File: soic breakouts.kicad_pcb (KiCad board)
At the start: 2 copper layers, 128.4 x 76 mm, 106 parts, among them J1 Conn_01x07, J2 Conn_01x07, J3 Conn_01x01, J4 Conn_01x08, J5 Conn_01x08, J6 Conn_01x01, U1 TL074, U2 LM13700

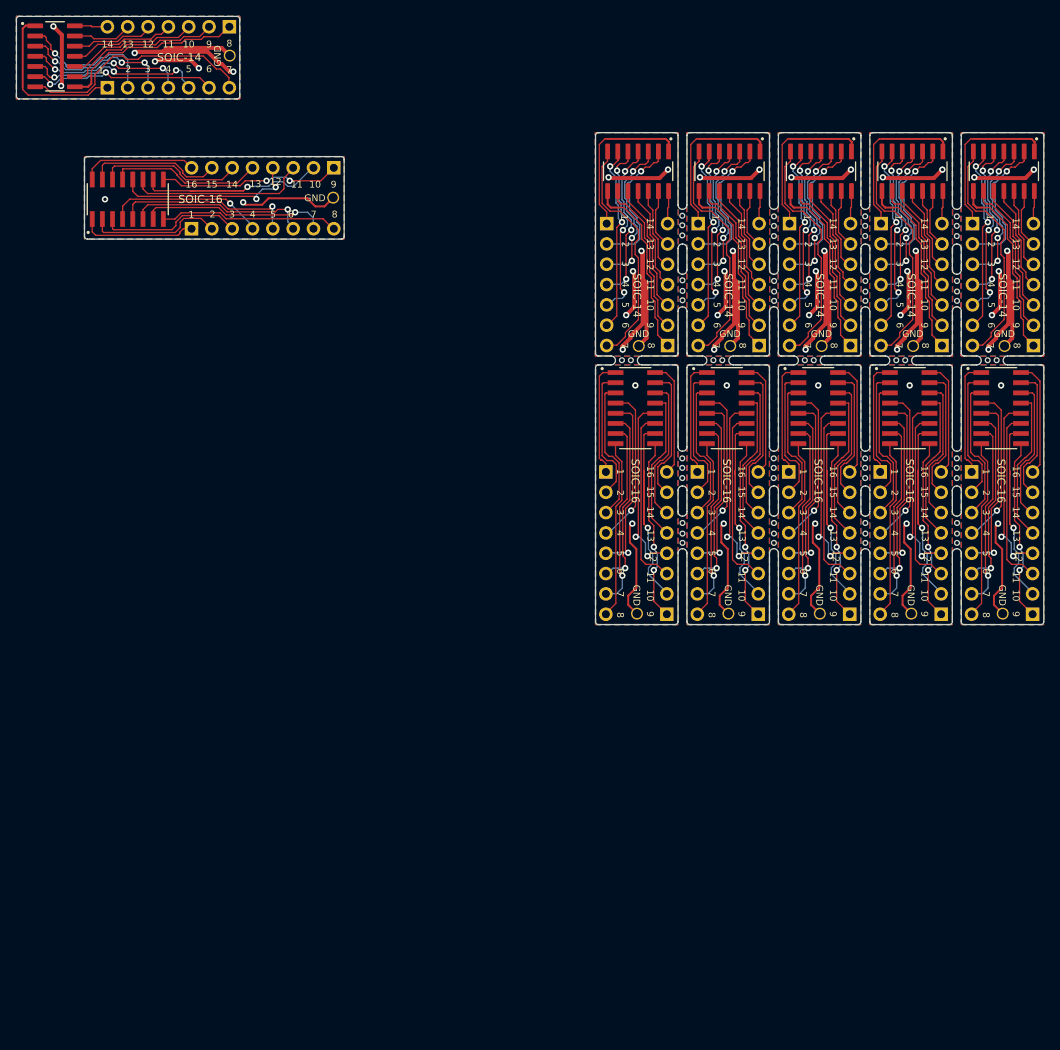
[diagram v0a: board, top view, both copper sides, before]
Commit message: Add SOIC-8.
* Update to KiCAD 8 format.
* Add SOIC-8 footprint breakout.
* Update to new IPC pin 1 (triangle/arrow) indicator throughout.
* Make pin 1 on header more obvious with IPC indicator throughout.
* Increase silkscreen font size for main label per breakout board.
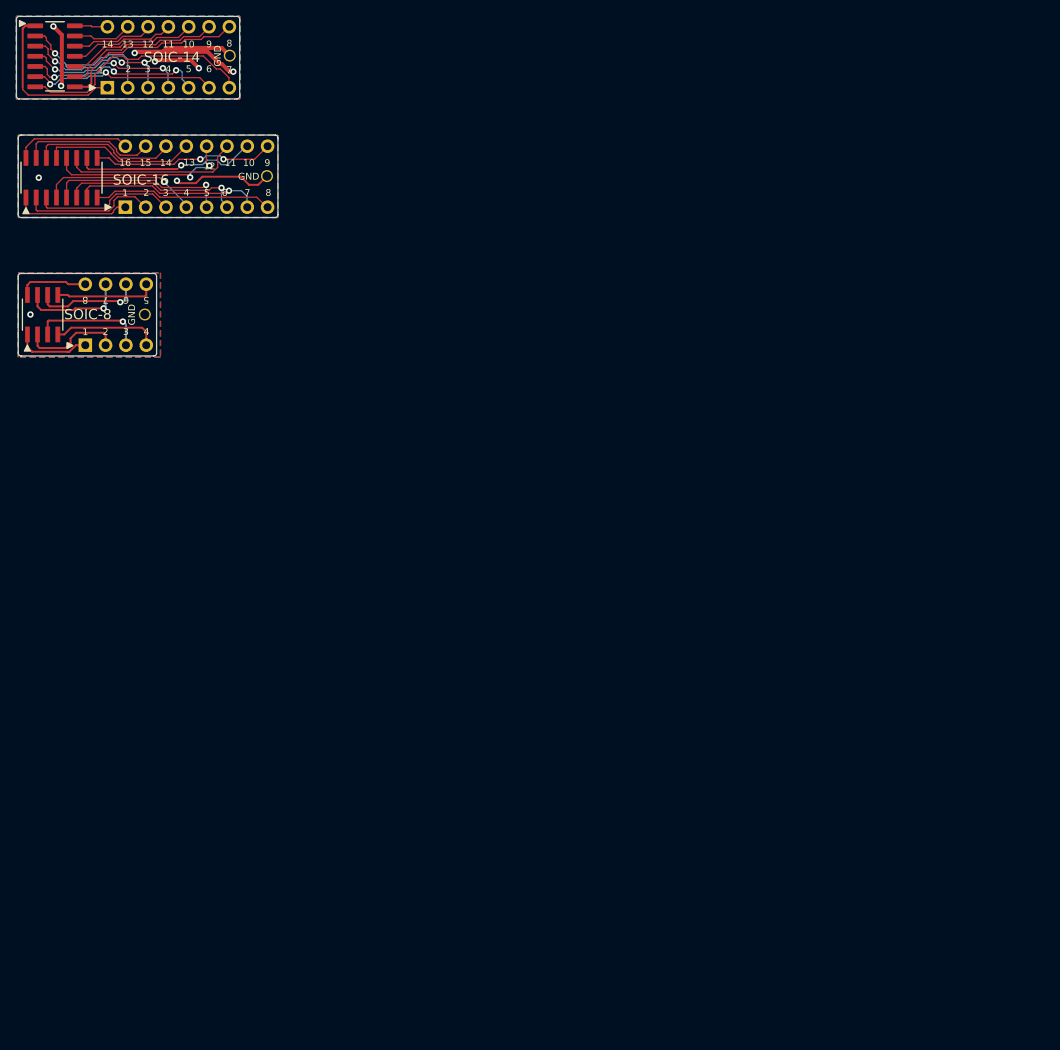
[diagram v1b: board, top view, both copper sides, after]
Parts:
- removed the J1 at (103.0, 41.9)
- removed the J1 at (137.3, 41.9)
- removed the J1 at (91.6, 41.9)
- removed the J1 at (125.9, 41.9)
- removed the J1 at (114.5, 41.9)
- removed the J2 at (133.5, 57.1)
- removed the J2 at (122.1, 57.1)
- removed the J2 at (144.9, 57.1)
- removed the J2 at (99.2, 57.1)
- removed the J2 at (110.6, 57.1)
- removed the J3 at (141.3, 57.1)
- removed the J3 at (129.9, 57.1)
- removed the J3 at (95.6, 57.1)
- removed the J3 at (118.5, 57.1)
- removed the J3 at (107.0, 57.1)
- removed the J4 at (102.9, 72.9)
- removed the J4 at (137.2, 72.9)
- removed the J4 at (114.4, 72.9)
- removed the J4 at (91.5, 72.9)
- removed the J4 at (125.8, 72.9)
- removed the J5 at (110.5, 90.7)
- removed the J5 at (133.4, 90.7)
- removed the J5 at (122.0, 90.7)
- removed the J5 at (99.1, 90.7)
- removed the J5 at (144.8, 90.7)
- removed the J6 at (95.4, 90.6)
- removed the J6 at (129.7, 90.6)
- removed the J6 at (118.2, 90.6)
- removed the J6 at (106.8, 90.6)
- removed the J6 at (141.1, 90.6)
- removed REF** (x58): MountingHole_80mil, Aaron_Pads:MountingHole_80mil
- removed the U1 at (129.8, 35.3)
- removed the U1 at (95.5, 35.3)
- removed the U1 at (106.9, 35.3)
- removed the U1 at (141.2, 35.3)
- removed the U1 at (118.4, 35.3)
- removed the U2 at (106.6, 64.9)
- removed the U2 at (140.9, 64.9)
- removed the U2 at (118.0, 64.9)
- removed the U2 at (95.2, 64.9)
- removed the U2 at (129.5, 64.9)
- added J7: Conn_01x01, Aaron_Pads:TP_HeaderPin_P2.54mm_round, F.Cu at (33.9, 53.2)
- added J8: Conn_01x04, Connector_PinHeader_2.54mm:PinHeader_1x04_P2.54mm_Vertical, F.Cu at (26.4, 49.4)
- added J9: Conn_01x04, Connector_PinHeader_2.54mm:PinHeader_1x04_P2.54mm_Vertical, F.Cu at (26.4, 57.0)
- added U3: TL072, Aaron_TI_Parts:TI_SOIC_D_R-PDSO-8, F.Cu at (21.1, 53.2)
- moved J4 8.71 mm to (31.4, 39.8)
- moved J5 8.71 mm to (49.2, 32.2)
- moved J6 8.71 mm to (49.1, 35.9)
- moved U2 8.71 mm to (23.4, 36.1)
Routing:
- net /GND1: track 235.1 -> 39.2 mm, vias 36 -> 6
- net Net-(J1-Pin_7): track 178.9 -> 29.8 mm
- net Net-(J5-Pin_2): track 176.3 -> 29.4 mm, vias 6 -> 1
- net Net-(J1-Pin_6): track 144.9 -> 24.2 mm, vias 12 -> 2
- net Net-(J4-Pin_7): track 137.1 -> 22.8 mm, vias 6 -> 1
- net Net-(J5-Pin_4): track 136.6 -> 22.8 mm, vias 12 -> 2
- net Net-(J2-Pin_1): track 135.8 -> 22.6 mm
- net Net-(J4-Pin_5): track 133.3 -> 22.2 mm, vias 6 -> 1
- net Net-(J1-Pin_5): track 133.1 -> 22.2 mm, vias 18 -> 3
- net Net-(J5-Pin_1): track 133.1 -> 22.2 mm, vias 12 -> 2
- net Net-(J4-Pin_6): track 132.3 -> 22.0 mm, vias 6 -> 1
- net Net-(J5-Pin_3): track 131.8 -> 22.0 mm
- net Net-(J4-Pin_8): track 130.7 -> 21.8 mm
- net Net-(J1-Pin_1): track 123.3 -> 20.6 mm
- net Net-(J1-Pin_4): track 121.9 -> 20.3 mm, vias 18 -> 3
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- added copper zone on B.Cu, net /GND3
- added copper zone on F.Cu, net /GND3
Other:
- board size 128.4 x 76 mm -> 32.7 x 42.4 mm
- board text added: "SOIC-8"

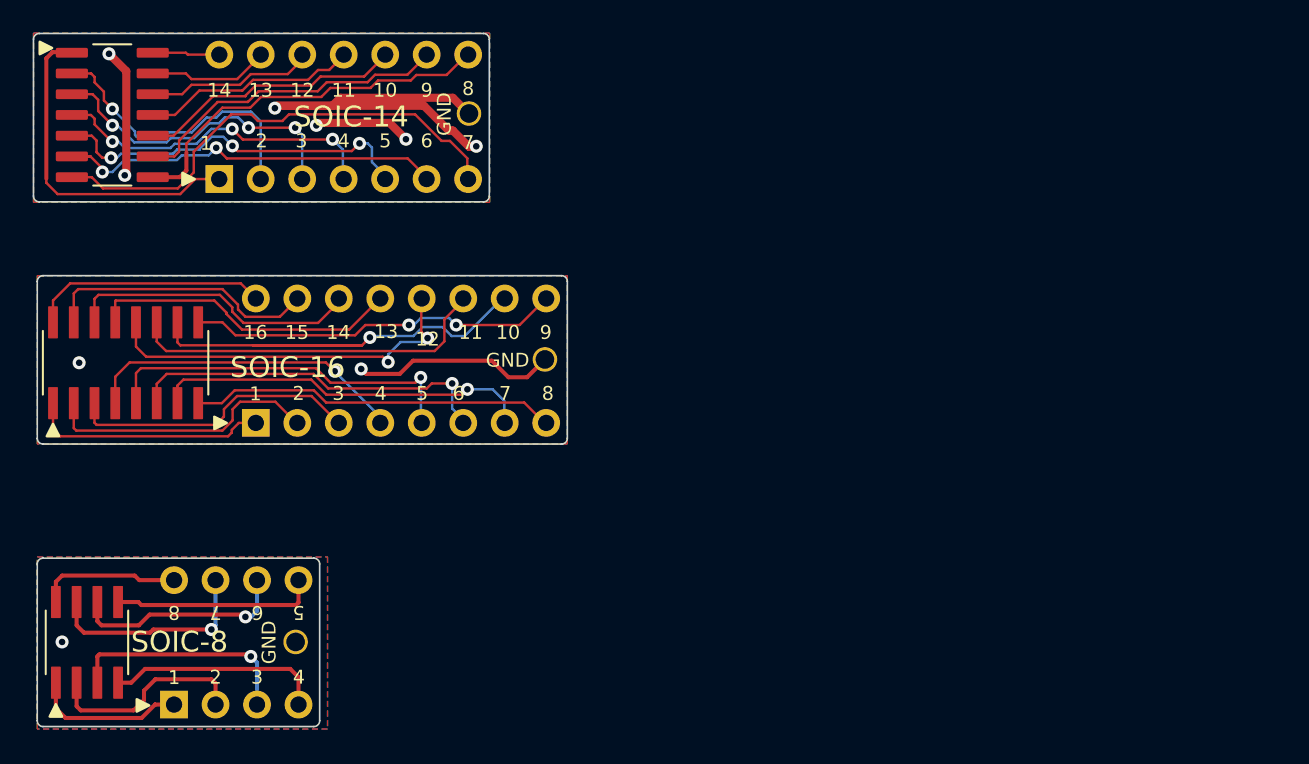
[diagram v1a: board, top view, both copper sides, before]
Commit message: Add TSSOP-8, -14, -16 breakouts.
Now have SOIC and TSSOP for 8/14/16 pin variants.
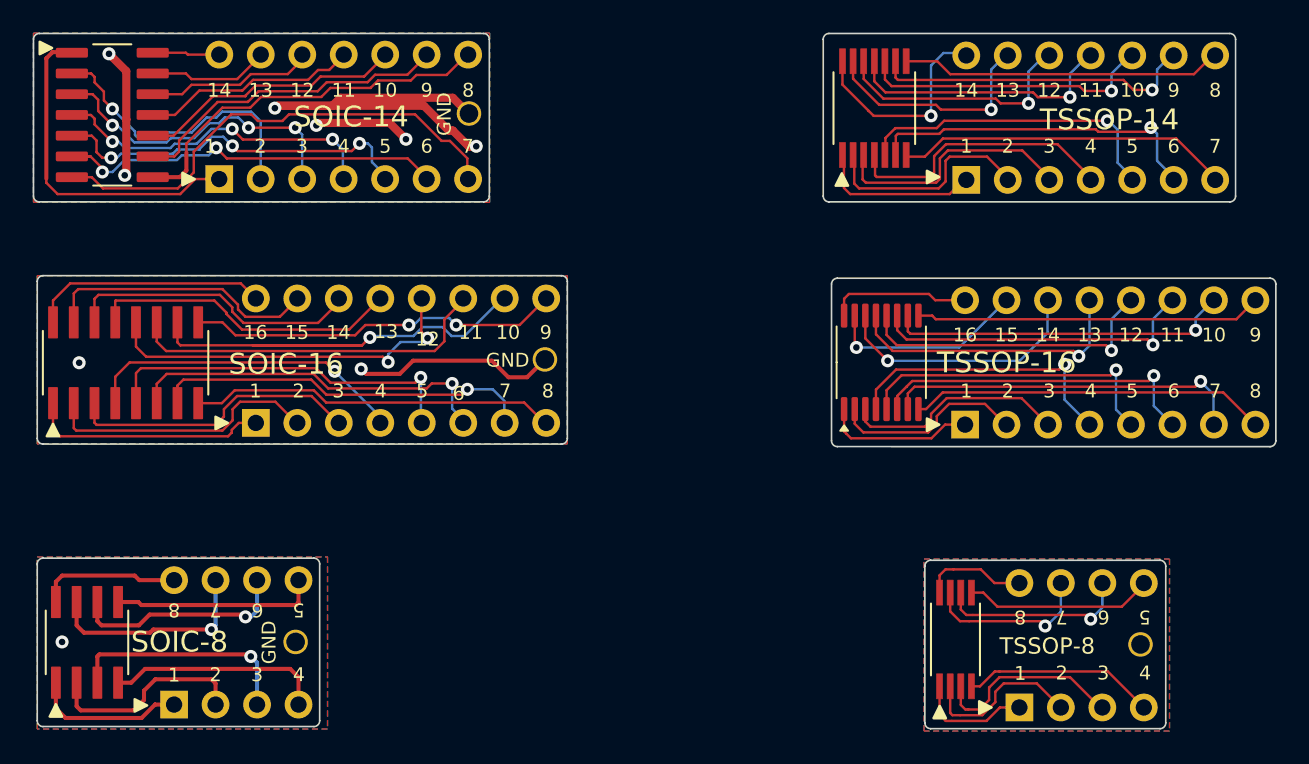
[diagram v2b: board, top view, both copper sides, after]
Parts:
- added J10: Conn_01x07, Connector_PinHeader_2.54mm:PinHeader_1x07_P2.54mm_Vertical, F.Cu at (90.2, 17.3)
- added J11: Conn_01x07, Connector_PinHeader_2.54mm:PinHeader_1x07_P2.54mm_Vertical, F.Cu at (74.9, 24.9)
- added J12: Conn_01x08, Connector_PinHeader_2.54mm:PinHeader_1x08_P2.54mm_Vertical, F.Cu at (92.6, 32.3)
- added J13: Conn_01x08, Connector_PinHeader_2.54mm:PinHeader_1x08_P2.54mm_Vertical, F.Cu at (74.9, 39.9)
- added J14: Conn_01x04, Connector_PinHeader_2.54mm:PinHeader_1x04_P2.54mm_Vertical, F.Cu at (78.2, 49.6)
- added J15: Conn_01x04, Connector_PinHeader_2.54mm:PinHeader_1x04_P2.54mm_Vertical, F.Cu at (78.2, 57.2)
- added J17: Conn_01x01, Aaron_Pads:TP_HeaderPin_P2.54mm_round, F.Cu at (85.6, 53.4)
- added U4: LM13700, Package_SO:TSSOP-16_4.4x5mm_P0.65mm, F.Cu at (69.7, 36.1)
- added U5: TL074, Aaron_TI_Parts:TI_TSSOP_PW0014A, F.Cu at (69.3, 20.5)
- added U6: TL072, Aaron_TI_Parts:TI_TSSOP_PW0008A, F.Cu at (74.3, 53.1)
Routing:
- net Net-(J13-Pin_7): track 0.00 -> 22.2 mm, vias 0 -> 1
- net Net-(J13-Pin_8): track 0.00 -> 21.9 mm
- net Net-(J12-Pin_1): track 0.00 -> 21.1 mm
- net Net-(J12-Pin_2): track 0.00 -> 21.0 mm, vias 0 -> 1
- net Net-(J11-Pin_6): track 0.00 -> 20.7 mm, vias 0 -> 1
- net Net-(J13-Pin_6): track 0.00 -> 20.5 mm, vias 0 -> 1
- net Net-(J11-Pin_7): track 0.00 -> 20.2 mm
- net Net-(J12-Pin_3): track 0.00 -> 20.1 mm, vias 0 -> 1
- net Net-(J10-Pin_2): track 0.00 -> 19.8 mm, vias 0 -> 1
- net Net-(J10-Pin_1): track 0.00 -> 19.8 mm
- net Net-(J13-Pin_5): track 0.00 -> 19.4 mm, vias 0 -> 1
- net Net-(J11-Pin_5): track 0.00 -> 19.2 mm, vias 0 -> 1
- net Net-(J12-Pin_4): track 0.00 -> 18.8 mm, vias 0 -> 1
- net Net-(J10-Pin_3): track 0.00 -> 18.1 mm, vias 0 -> 1
- net Net-(J12-Pin_5): track 0.00 -> 17.8 mm, vias 0 -> 1
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- added copper zone on B.Cu, net /GND6
- added copper zone on F.Cu, net /GND6
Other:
- board size 32.7 x 42.4 mm -> 76.1 x 42.6 mm
- board text added: "TSSOP-14"
- board text added: "TSSOP-16"
- board text added: "TSSOP-8"

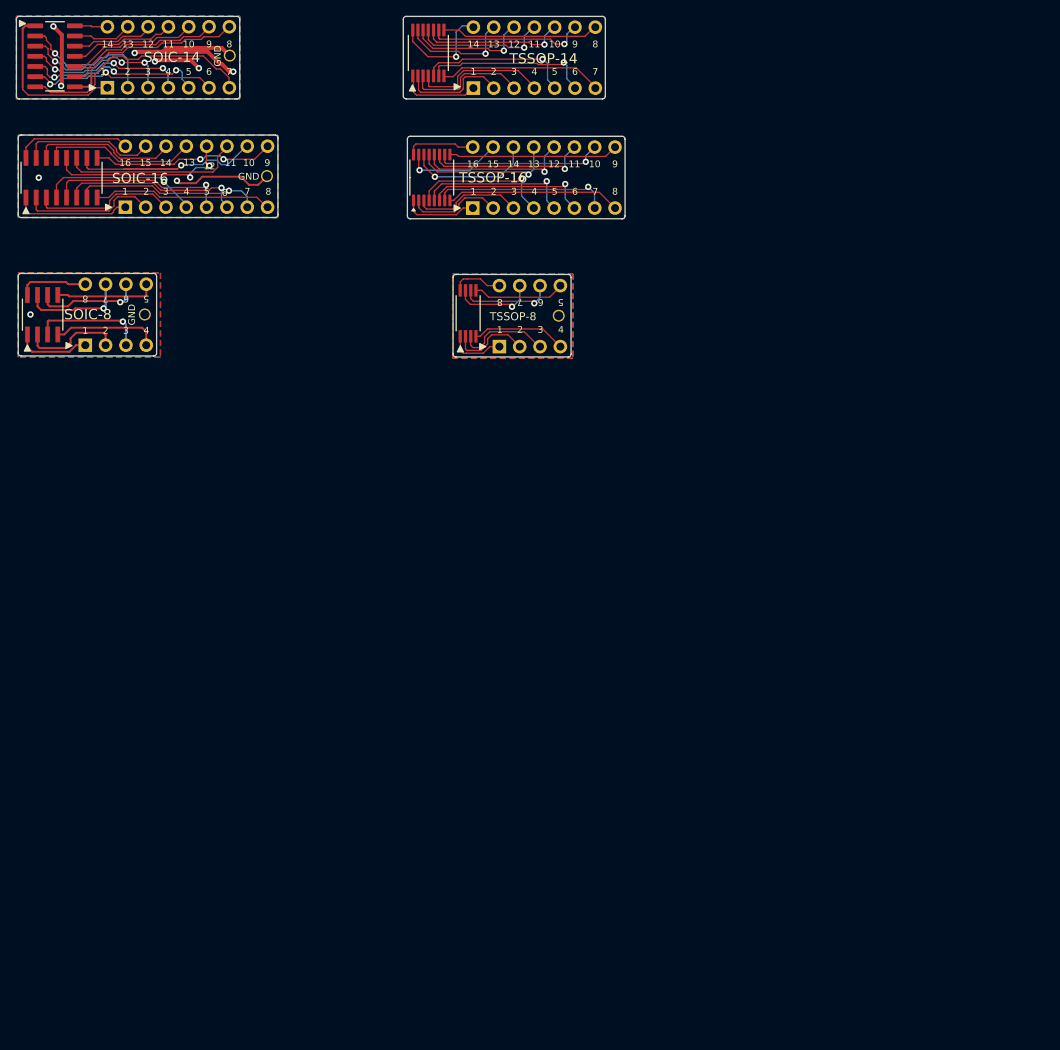
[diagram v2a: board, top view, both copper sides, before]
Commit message: Add KiKit panelization script.
Added python script using KiKit SDK to generate separate
SOIC and TSSOP breakout board panels.
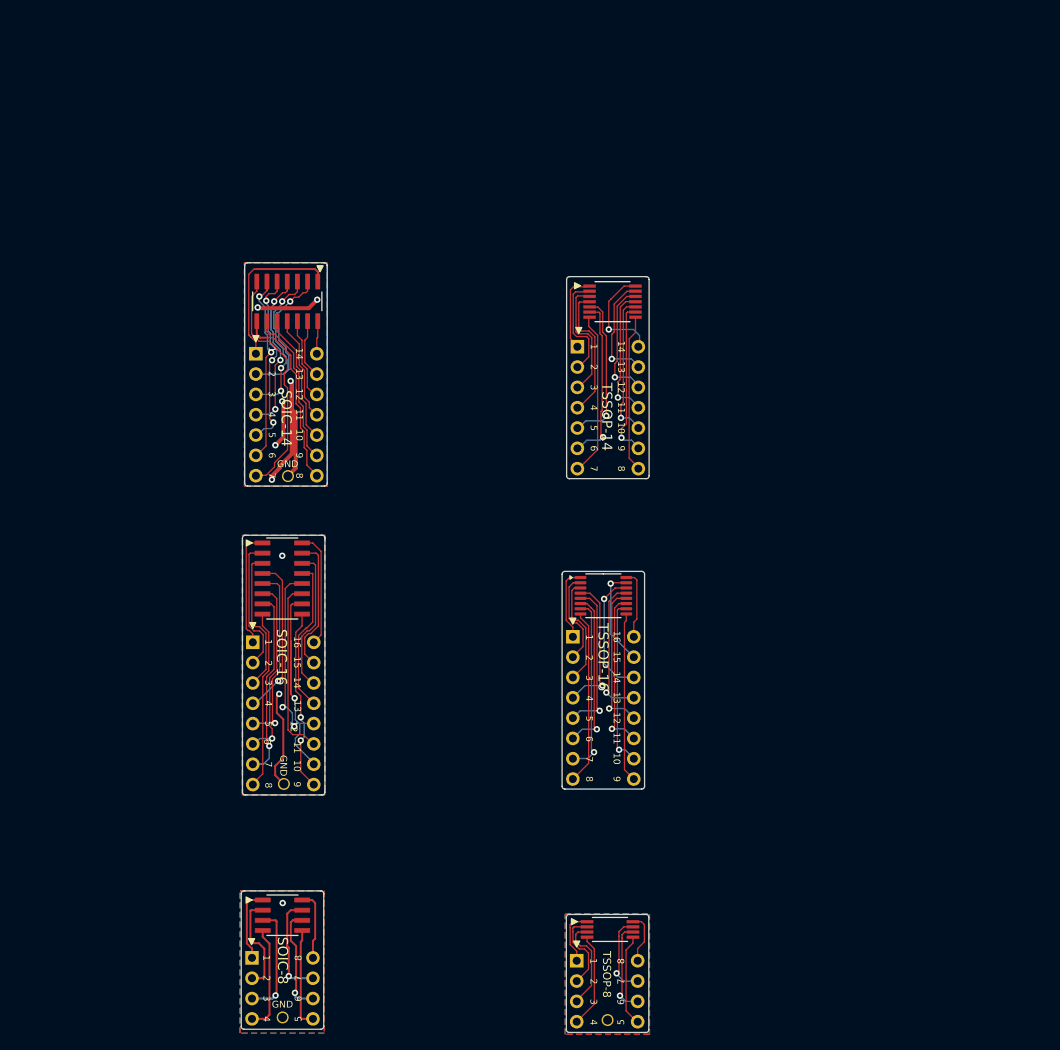
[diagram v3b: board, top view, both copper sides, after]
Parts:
- added B1: Board, PCM_kikit:Board, F.Cu at (56.7, 52.8)
- added B2: Board, PCM_kikit:Board, F.Cu at (56.4, 88.0)
- added B3: Board, PCM_kikit:Board, F.Cu at (56.2, 130.7)
- added B4: Board, PCM_kikit:Board, F.Cu at (96.9, 53.2)
- added B5: Board, PCM_kikit:Board, F.Cu at (96.3, 90.7)
- added B6: Board, PCM_kikit:Board, F.Cu at (96.9, 129.1)
- moved J7 89.5 mm to (51.1, 141.1), turned to -90 degrees
- moved J8 88.9 mm to (54.9, 133.6), turned to 0 degrees
- moved J17 88.3 mm to (91.7, 141.4), turned to 180 degrees
- moved J14 86.1 mm to (95.5, 134.0), turned to 0 degrees
- moved U3 80.8 mm to (51.1, 128.3), turned to 0 degrees
- moved J5 80.0 mm to (55.0, 112.0), turned to 180 degrees
- moved J9 79.4 mm to (47.3, 133.6), turned to 0 degrees
- moved U6 79.0 mm to (92.0, 130.1), turned to 0 degrees
- moved J12 79.0 mm to (95.0, 111.3), turned to 180 degrees
- moved J15 77.4 mm to (87.8, 134.0), turned to 0 degrees
- moved J6 76.0 mm to (51.2, 111.9), turned to -90 degrees
- moved U2 57.2 mm to (51.0, 86.2), turned to 0 degrees
- moved J2 57.2 mm to (55.4, 73.4), turned to 180 degrees
- moved J4 56.7 mm to (47.4, 94.2), turned to 0 degrees
- moved U4 56.5 mm to (91.2, 88.4), turned to 0 degrees
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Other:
- board size 76.1 x 42.6 mm -> 51 x 96.2 mm
